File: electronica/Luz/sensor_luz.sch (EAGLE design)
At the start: 13 parts

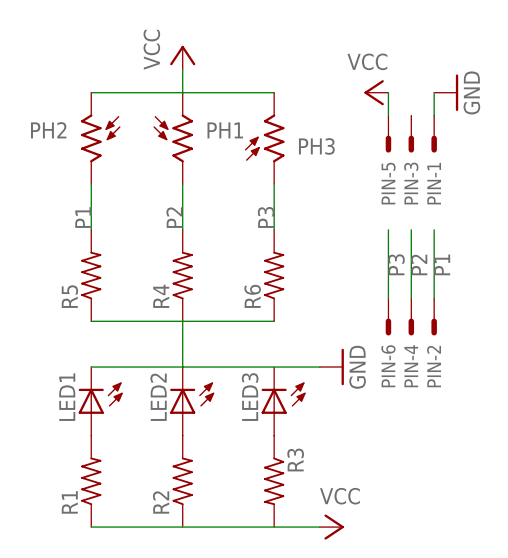
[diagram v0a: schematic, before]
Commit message: electronica diseño placa luz
diseño de la placa del sensor de luz
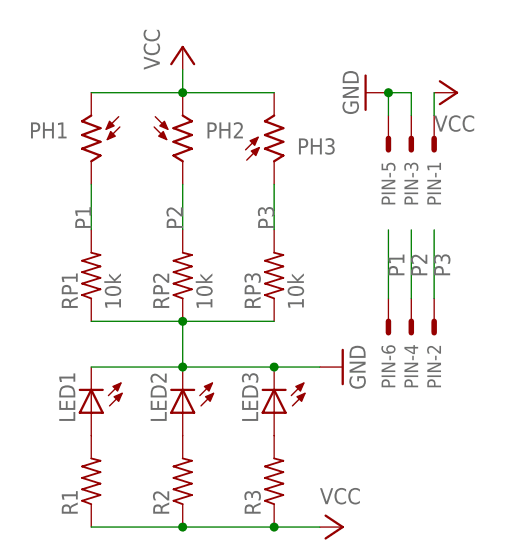
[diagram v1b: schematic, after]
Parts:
- RP1, RP2, RP3: value (none) -> 10k
- renumbered R4 to RP2, R5 to RP1, R6 to RP3
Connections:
- net GND: now also LED2.C, LED3.C, PIN-3.S, PIN-5.S; no longer PIN-1.S
- net N$3: now also R3.2; no longer R3.1
- net P1: now also PH1.2, PIN-6.S; no longer PH2.2, PIN-2.S
- net P2: now also PH2.2; no longer PH1.2
- net P3: now also PIN-2.S; no longer PIN-6.S
- net VCC: now also PIN-1.S, R2.1, R3.1; no longer PIN-5.S
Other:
- moved on the sheet: PH1, PH2, R3
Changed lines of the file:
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@@
 <part name="R2" library="rcl" deviceset="R-US_" device="0207/7"/>
 <part name="R3" library="rcl" deviceset="R-US_" device="0207/7"/>
+<part name="PH2" library="photo-elements" deviceset="VT2*" device="" technology="0N4" value=""/>
 <part name="PH1" library="photo-elements" deviceset="VT2*" device="" technology="0N4" value=""/>
-<part name="PH2" library="photo-elements" deviceset="VT2*" device="" technology="0N4" value=""/>
 <part name="PH3" library="photo-elements" deviceset="VT2*" device="" technology="0N4" value=""/>
 <part name="GND1" library="supply1" deviceset="GND" device=""/>
@@
 <part name="GND2" library="supply1" deviceset="GND" device=""/>
 <part name="P+3" library="supply1" deviceset="VCC" device=""/>
-<part name="R4" library="rcl" deviceset="R-US_" device="0207/7"/>
-<part name="R5" library="rcl" deviceset="R-US_" device="0207/7"/>
-<part name="R6" library="rcl" deviceset="R-US_" device="0207/7"/>
+<part name="RP2" library="rcl" deviceset="R-US_" device="0207/7" value="10k"/>
+<part name="RP1" library="rcl" deviceset="R-US_" device="0207/7" value="10k"/>
+<part name="RP3" library="rcl" deviceset="R-US_" device="0207/7" value="10k"/>
 </parts>
 <sheets>
@@
 <instance part="R1" gate="G$1" x="12.7" y="68.58" rot="R90"/>
 <instance part="R2" gate="G$1" x="22.86" y="68.58" rot="R90"/>
-<instance part="R3" gate="G$1" x="33.02" y="68.58" rot="R270"/>
-<instance part="PH1" gate="G$1" x="22.86" y="106.68"/>
-<instance part="PH2" gate="G$1" x="12.7" y="106.68" rot="MR0"/>
+<instance part="R3" gate="G$1" x="33.02" y="68.58" rot="R90"/>
+<instance part="PH2" gate="G$1" x="22.86" y="106.68"/>
+<instance part="PH1" gate="G$1" x="12.7" y="106.68" rot="MR0"/>
 <instance part="PH3" gate="G$1" x="33.02" y="106.68" rot="MR180"/>
 <instance part="GND1" gate="1" x="40.64" y="81.28" rot="R90"/>
@@
 <instance part="PIN" gate="-5" x="45.72" y="106.68" rot="R270"/>
 <instance part="PIN" gate="-6" x="45.72" y="86.36" rot="R270"/>
-<instance part="GND2" gate="1" x="53.34" y="111.76" rot="R90"/>
-<instance part="P+3" gate="VCC" x="43.18" y="111.76" rot="MR270"/>
-<instance part="R4" gate="G$1" x="22.86" y="91.44" rot="R90"/>
-<instance part="R5" gate="G$1" x="12.7" y="91.44" rot="R90"/>
-<instance part="R6" gate="G$1" x="33.02" y="91.44" rot="R90"/>
+<instance part="GND2" gate="1" x="43.18" y="111.76" rot="R270"/>
+<instance part="P+3" gate="VCC" x="53.34" y="111.76" rot="MR90"/>
+<instance part="RP2" gate="G$1" x="22.86" y="91.44" rot="R90"/>
+<instance part="RP1" gate="G$1" x="12.7" y="91.44" rot="R90"/>
+<instance part="RP3" gate="G$1" x="33.02" y="91.44" rot="R90"/>
 </instances>
 <busses>
@@
 <pinref part="GND1" gate="1" pin="GND"/>
 <wire x1="12.7" y1="81.28" x2="22.86" y2="81.28" width="0.1524" layer="91"/>
-<pinref part="R5" gate="G$1" pin="1"/>
-<pinref part="R4" gate="G$1" pin="1"/>
-<wire x1="22.86" y1="81.28" x2="38.1" y2="81.28" width="0.1524" layer="91"/>
+<pinref part="RP1" gate="G$1" pin="1"/>
+<pinref part="RP2" gate="G$1" pin="1"/>
+<wire x1="22.86" y1="81.28" x2="33.02" y2="81.28" width="0.1524" layer="91"/>
+<wire x1="33.02" y1="81.28" x2="38.1" y2="81.28" width="0.1524" layer="91"/>
 <wire x1="12.7" y1="86.36" x2="22.86" y2="86.36" width="0.1524" layer="91"/>
-<pinref part="R6" gate="G$1" pin="1"/>
+<pinref part="RP3" gate="G$1" pin="1"/>
 <wire x1="22.86" y1="86.36" x2="33.02" y2="86.36" width="0.1524" layer="91"/>
 <wire x1="22.86" y1="86.36" x2="22.86" y2="81.28" width="0.1524" layer="91"/>
+<junction x="22.86" y="86.36"/>
+<pinref part="LED3" gate="G$1" pin="C"/>
+<junction x="33.02" y="81.28"/>
+<pinref part="LED2" gate="G$1" pin="C"/>
+<junction x="22.86" y="81.28"/>
 </segment>
 <segment>
 <pinref part="GND2" gate="1" pin="GND"/>
-<pinref part="PIN" gate="-1" pin="S"/>
-<wire x1="50.8" y1="109.22" x2="50.8" y2="111.76" width="0.1524" layer="91"/>
+<pinref part="PIN" gate="-5" pin="S"/>
+<wire x1="45.72" y1="111.76" x2="45.72" y2="109.22" width="0.1524" layer="91"/>
+<pinref part="PIN" gate="-3" pin="S"/>
+<wire x1="48.26" y1="109.22" x2="48.26" y2="111.76" width="0.1524" layer="91"/>
+<wire x1="48.26" y1="111.76" x2="45.72" y2="111.76" width="0.1524" layer="91"/>
+<junction x="45.72" y="111.76"/>
 </segment>
 </net>
@@
 </segment>
 </net>
-<net name="N$3" class="0">
-<segment>
-<pinref part="LED3" gate="G$1" pin="A"/>
-<pinref part="R3" gate="G$1" pin="1"/>
-</segment>
-</net>
 <net name="VCC" class="0">
 <segment>
-<pinref part="R1" gate="G$1" pin="1"/>
-<pinref part="P+1" gate="VCC" pin="VCC"/>
-<wire x1="12.7" y1="63.5" x2="38.1" y2="63.5" width="0.1524" layer="91"/>
-</segment>
-<segment>
-<pinref part="PIN" gate="-5" pin="S"/>
-<pinref part="P+3" gate="VCC" pin="VCC"/>
-<wire x1="45.72" y1="111.76" x2="45.72" y2="109.22" width="0.1524" layer="91"/>
-</segment>
-<segment>
+<pinref part="PH1" gate="G$1" pin="1"/>
 <pinref part="PH2" gate="G$1" pin="1"/>
-<pinref part="PH1" gate="G$1" pin="1"/>
 <wire x1="12.7" y1="111.76" x2="22.86" y2="111.76" width="0.1524" layer="91"/>
 <pinref part="P+2" gate="VCC" pin="VCC"/>
@@
 <pinref part="PH3" gate="G$1" pin="2"/>
 <wire x1="22.86" y1="111.76" x2="33.02" y2="111.76" width="0.1524" layer="91"/>
+<junction x="22.86" y="111.76"/>
+</segment>
+<segment>
+<pinref part="R1" gate="G$1" pin="1"/>
+<pinref part="R2" gate="G$1" pin="1"/>
+<wire x1="12.7" y1="63.5" x2="22.86" y2="63.5" width="0.1524" layer="91"/>
+<pinref part="R3" gate="G$1" pin="1"/>
+<wire x1="22.86" y1="63.5" x2="33.02" y2="63.5" width="0.1524" layer="91"/>
+<pinref part="P+1" gate="VCC" pin="VCC"/>
+<wire x1="33.02" y1="63.5" x2="38.1" y2="63.5" width="0.1524" layer="91"/>
+<junction x="22.86" y="63.5"/>
+<junction x="33.02" y="63.5"/>
+</segment>
+<segment>
+<pinref part="P+3" gate="VCC" pin="VCC"/>
+<pinref part="PIN" gate="-1" pin="S"/>
+<wire x1="50.8" y1="111.76" x2="50.8" y2="109.22" width="0.1524" layer="91"/>
 </segment>
 </net>
@@
 <segment>
 <pinref part="PH3" gate="G$1" pin="1"/>
-<pinref part="R6" gate="G$1" pin="2"/>
+<pinref part="RP3" gate="G$1" pin="2"/>
 <wire x1="33.02" y1="101.6" x2="33.02" y2="96.52" width="0.1524" layer="91"/>
 <label x="33.02" y="96.52" size="1.778" layer="95" rot="R90"/>
+</segment>
+<segment>
+<pinref part="PIN" gate="-2" pin="S"/>
+<wire x1="50.8" y1="88.9" x2="50.8" y2="96.52" width="0.1524" layer="91"/>
+<label x="50.8" y="93.98" size="1.778" layer="95" rot="R270"/>
+</segment>
+</net>
+<net name="P1" class="0">
+<segment>
+<pinref part="PH1" gate="G$1" pin="2"/>
+<wire x1="12.7" y1="101.6" x2="12.7" y2="96.52" width="0.1524" layer="91"/>
+<label x="12.7" y="96.52" size="1.778" layer="95" rot="R90"/>
+<pinref part="RP1" gate="G$1" pin="2"/>
 </segment>
 <segment>
@@
 </segment>
 </net>
-<net name="P1" class="0">
+<net name="P2" class="0">
 <segment>
 <pinref part="PH2" gate="G$1" pin="2"/>
-<wire x1="12.7" y1="101.6" x2="12.7" y2="96.52" width="0.1524" layer="91"/>
-<label x="12.7" y="96.52" size="1.778" layer="95" rot="R90"/>
-<pinref part="R5" gate="G$1" pin="2"/>
-</segment>
-<segment>
-<pinref part="PIN" gate="-2" pin="S"/>
-<wire x1="50.8" y1="88.9" x2="50.8" y2="96.52" width="0.1524" layer="91"/>
-<label x="50.8" y="93.98" size="1.778" layer="95" rot="R270"/>
-</segment>
-</net>
-<net name="P2" class="0">
-<segment>
-<pinref part="PH1" gate="G$1" pin="2"/>
 <wire x1="22.86" y1="101.6" x2="22.86" y2="96.52" width="0.1524" layer="91"/>
 <label x="22.86" y="96.52" size="1.778" layer="95" rot="R90"/>
-<pinref part="R4" gate="G$1" pin="2"/>
+<pinref part="RP2" gate="G$1" pin="2"/>
 </segment>
 <segment>
@@
 </segment>
 </net>
+<net name="N$3" class="0">
+<segment>
+<pinref part="LED3" gate="G$1" pin="A"/>
+<pinref part="R3" gate="G$1" pin="2"/>
+</segment>
+</net>
 </nets>
 </sheet>
 </sheets>
+<errors>
+</errors>
 </schematic>
 </drawing>
